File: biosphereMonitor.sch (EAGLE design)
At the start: 34 parts, among them IC1 XMEGA32A4AU, IC2 LM35, IC3 FT232RL, Q1 16Mhz, Q2 32kHz

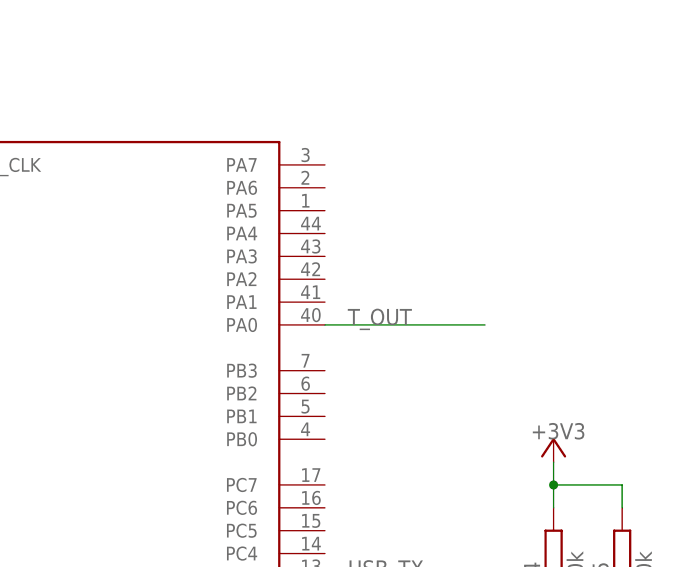
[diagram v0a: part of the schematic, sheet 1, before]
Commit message: added adc input for humidity and illuminance
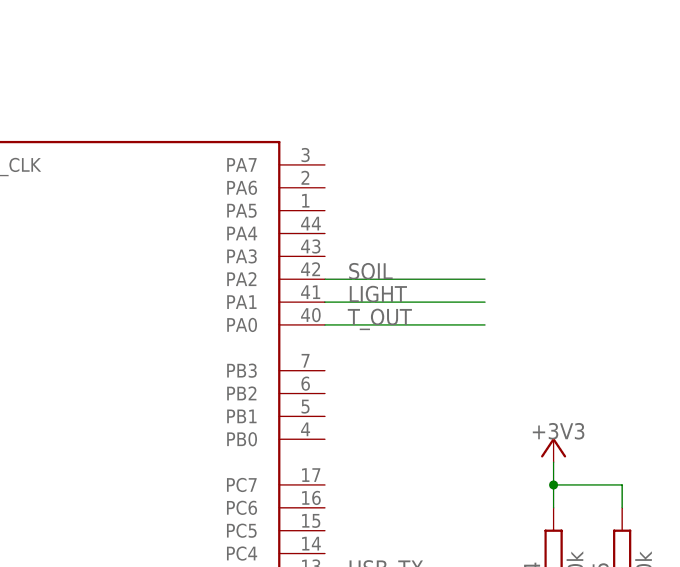
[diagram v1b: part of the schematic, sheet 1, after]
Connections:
- new net LIGHT: IC1.PA1
- new net SOIL: IC1.PA2
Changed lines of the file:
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@@
+</segment>
+</net>
+<net name="LIGHT" class="0">
+<segment>
+<pinref part="IC1" gate="G$1" pin="PA1"/>
+<wire x1="27.94" y1="22.86" x2="45.72" y2="22.86" width="0.1524" layer="91"/>
+<label x="30.48" y="22.86" size="1.778" layer="95"/>
+</segment>
+</net>
+<net name="SOIL" class="0">
+<segment>
+<pinref part="IC1" gate="G$1" pin="PA2"/>
+<wire x1="27.94" y1="25.4" x2="45.72" y2="25.4" width="0.1524" layer="91"/>
+<label x="30.48" y="25.4" size="1.778" layer="95"/>
 </segment>
 </net>

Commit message: Defined Board Shape
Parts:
- added JP4: SOIL, pinhead:PINHD-1X3
- JP2: value (none) -> PDI
- JP3: value (none) -> BME
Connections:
- net +5V: now also JP4.2
- net GND: now also JP4.3
- net SOIL: now also JP4.1
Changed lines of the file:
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@@
 <parts>
 <part name="IC1" library="atmel" library_urn="urn:adsk.eagle:library:105" deviceset="XMEGA16A4" device="A" package3d_urn="urn:adsk.eagle:package:4319/1" value="XMEGA32A4AU"/>
-<part name="JP2" library="con-harting-ml" library_urn="urn:adsk.eagle:library:149" deviceset="ML10" device="L" package3d_urn="urn:adsk.eagle:package:6964/1"/>
+<part name="JP2" library="con-harting-ml" library_urn="urn:adsk.eagle:library:149" deviceset="ML10" device="L" package3d_urn="urn:adsk.eagle:package:6964/1" value="PDI"/>
 <part name="GND1" library="supply1" library_urn="urn:adsk.eagle:library:371" deviceset="GND" device=""/>
 <part name="+3V1" library="supply1" library_urn="urn:adsk.eagle:library:371" deviceset="+3V3" device=""/>
@@
 <part name="R2" library="rcl" library_urn="urn:adsk.eagle:library:334" deviceset="R-EU_" device="R0805" package3d_urn="urn:adsk.eagle:package:23553/2" value="0"/>
 <part name="R3" library="rcl" library_urn="urn:adsk.eagle:library:334" deviceset="R-EU_" device="R0805" package3d_urn="urn:adsk.eagle:package:23553/2" value="0"/>
-<part name="JP3" library="pinhead" library_urn="urn:adsk.eagle:library:325" deviceset="PINHD-1X4" device="" package3d_urn="urn:adsk.eagle:package:22407/2"/>
+<part name="JP3" library="pinhead" library_urn="urn:adsk.eagle:library:325" deviceset="PINHD-1X4" device="" package3d_urn="urn:adsk.eagle:package:22407/2" value="BME"/>
 <part name="GND10" library="supply1" library_urn="urn:adsk.eagle:library:371" deviceset="GND" device=""/>
 <part name="+3V7" library="supply1" library_urn="urn:adsk.eagle:library:371" deviceset="+3V3" device=""/>
@@
 <part name="TP5" library="testpad" library_urn="urn:adsk.eagle:library:385" deviceset="PTR1" device="B2,54" package3d_urn="urn:adsk.eagle:package:27948/1"/>
 <part name="TP6" library="testpad" library_urn="urn:adsk.eagle:library:385" deviceset="PTR1" device="B2,54" package3d_urn="urn:adsk.eagle:package:27948/1"/>
+<part name="JP4" library="pinhead" library_urn="urn:adsk.eagle:library:325" deviceset="PINHD-1X3" device="" package3d_urn="urn:adsk.eagle:package:22458/2" value="SOIL"/>
+<part name="GND12" library="supply1" library_urn="urn:adsk.eagle:library:371" deviceset="GND" device=""/>
+<part name="P+6" library="supply1" library_urn="urn:adsk.eagle:library:371" deviceset="+5V" device=""/>
 </parts>
 <sheets>
@@
 </sheet>
 <sheet>
+<description>Inside Sensors</description>
 <plain>
 </plain>
@@
 <attribute name="VALUE" x="-25.4" y="20.32" size="1.778" layer="96"/>
 </instance>
+<instance part="JP4" gate="A" x="2.54" y="-20.32" smashed="yes">
+<attribute name="NAME" x="-3.81" y="-14.605" size="1.778" layer="95"/>
+<attribute name="VALUE" x="-3.81" y="-27.94" size="1.778" layer="96"/>
+</instance>
+<instance part="GND12" gate="1" x="-22.86" y="-27.94" smashed="yes">
+<attribute name="VALUE" x="-25.4" y="-30.48" size="1.778" layer="96"/>
+</instance>
+<instance part="P+6" gate="1" x="-22.86" y="-10.16" smashed="yes">
+<attribute name="VALUE" x="-25.4" y="-10.16" size="1.778" layer="96"/>
+</instance>
 </instances>
 <busses>
@@
 <wire x1="-22.86" y1="5.08" x2="-22.86" y2="12.7" width="0.1524" layer="91"/>
 </segment>
-</net>
+<segment>
+<pinref part="JP4" gate="A" pin="3"/>
+<pinref part="GND12" gate="1" pin="GND"/>
+<wire x1="0" y1="-22.86" x2="-22.86" y2="-22.86" width="0.1524" layer="91"/>
+<wire x1="-22.86" y1="-22.86" x2="-22.86" y2="-25.4" width="0.1524" layer="91"/>
+</segment>
+</net>
+<net name="+5V" class="0">
+<segment>
+<pinref part="JP4" gate="A" pin="2"/>
+<pinref part="P+6" gate="1" pin="+5V"/>
+<wire x1="0" y1="-20.32" x2="-22.86" y2="-20.32" width="0.1524" layer="91"/>
+<wire x1="-22.86" y1="-20.32" x2="-22.86" y2="-12.7" width="0.1524" layer="91"/>
+</segment>
+</net>
+<net name="SOIL" class="0">
+<segment>
+<pinref part="JP4" gate="A" pin="1"/>
+<wire x1="0" y1="-17.78" x2="-20.32" y2="-17.78" width="0.1524" layer="91"/>
+<label x="-20.32" y="-17.78" size="1.778" layer="95"/>
+</segment>
+</net>

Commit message: added light sensor to schematic
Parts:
- added D1: LM4050 2.5, Tjarks_Bauteile (1):LM4040
- added PH1: BPW 96C TEL, photo-elements:A1050_13
- added R6: 1k, rcl:R-EU_R0805
- added R7: 2k2, rcl:R-EU_R0805
- added R8: 3k3, rcl:R-EU_R0805
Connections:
- new net 2.5V: D1.C, R6.1, R8.2
- net +5V: now also R6.2
- net GND: now also D1.A, PH1.2, R7.1
- net LIGHT: now also PH1.1, R7.2, R8.1
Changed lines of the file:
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@@
 <part name="GND12" library="supply1" library_urn="urn:adsk.eagle:library:371" deviceset="GND" device=""/>
 <part name="P+6" library="supply1" library_urn="urn:adsk.eagle:library:371" deviceset="+5V" device=""/>
+<part name="D1" library="Tjarks_Bauteile (1)" deviceset="LM4040" device="" value="LM4050 2.5"/>
+<part name="GND13" library="supply1" library_urn="urn:adsk.eagle:library:371" deviceset="GND" device=""/>
+<part name="R6" library="rcl" library_urn="urn:adsk.eagle:library:334" deviceset="R-EU_" device="R0805" package3d_urn="urn:adsk.eagle:package:23553/2" value="1k"/>
+<part name="P+7" library="supply1" library_urn="urn:adsk.eagle:library:371" deviceset="+5V" device=""/>
+<part name="PH1" library="photo-elements" library_urn="urn:adsk.eagle:library:323" deviceset="A10" device="" package3d_urn="urn:adsk.eagle:package:22201/1" technology="50_13" value="BPW 96C TEL"/>
+<part name="R7" library="rcl" library_urn="urn:adsk.eagle:library:334" deviceset="R-EU_" device="R0805" package3d_urn="urn:adsk.eagle:package:23553/2" value="2k2"/>
+<part name="R8" library="rcl" library_urn="urn:adsk.eagle:library:334" deviceset="R-EU_" device="R0805" package3d_urn="urn:adsk.eagle:package:23553/2" value="3k3"/>
+<part name="GND14" library="supply1" library_urn="urn:adsk.eagle:library:371" deviceset="GND" device=""/>
 </parts>
 <sheets>
@@
 <attribute name="NAME" x="-34.29" y="-9.144" size="1.778" layer="95"/>
 <attribute name="TP_SIGNAL_NAME" x="-29.21" y="-2.54" size="1.778" layer="97"/>
+</instance>
+<instance part="D1" gate="G$1" x="71.12" y="-17.78" smashed="yes" rot="R90">
+<attribute name="NAME" x="68.4784" y="-20.7264" size="1.778" layer="95" rot="R90"/>
+<attribute name="VALUE" x="74.2696" y="-22.2758" size="1.778" layer="96"/>
+</instance>
+<instance part="GND13" gate="1" x="71.12" y="-27.94" smashed="yes">
+<attribute name="VALUE" x="68.58" y="-30.48" size="1.778" layer="96"/>
+</instance>
+<instance part="R6" gate="G$1" x="71.12" y="-2.54" smashed="yes" rot="R90">
+<attribute name="NAME" x="69.6214" y="-6.35" size="1.778" layer="95" rot="R90"/>
+<attribute name="VALUE" x="74.422" y="-6.35" size="1.778" layer="96" rot="R90"/>
+</instance>
+<instance part="P+7" gate="1" x="71.12" y="7.62" smashed="yes">
+<attribute name="VALUE" x="68.58" y="7.62" size="1.778" layer="96"/>
 </instance>
 </instances>
@@
 <wire x1="-45.72" y1="2.54" x2="-45.72" y2="5.08" width="0.1524" layer="91"/>
 </segment>
+<segment>
+<pinref part="GND13" gate="1" pin="GND"/>
+<pinref part="D1" gate="G$1" pin="A"/>
+<wire x1="71.12" y1="-25.4" x2="71.12" y2="-20.32" width="0.1524" layer="91"/>
+</segment>
 </net>
 <net name="+3V3" class="0">
@@
 <wire x1="-30.48" y1="2.54" x2="-30.48" y2="5.08" width="0.1524" layer="91"/>
 </segment>
+<segment>
+<pinref part="R6" gate="G$1" pin="2"/>
+<pinref part="P+7" gate="1" pin="+5V"/>
+<wire x1="71.12" y1="2.54" x2="71.12" y2="5.08" width="0.1524" layer="91"/>
+</segment>
+</net>
+<net name="2.5V" class="0">
+<segment>
+<pinref part="D1" gate="G$1" pin="C"/>
+<pinref part="R6" gate="G$1" pin="1"/>
+<wire x1="71.12" y1="-15.24" x2="71.12" y2="-10.16" width="0.1524" layer="91"/>
+<wire x1="71.12" y1="-10.16" x2="71.12" y2="-7.62" width="0.1524" layer="91"/>
+<wire x1="71.12" y1="-10.16" x2="81.28" y2="-10.16" width="0.1524" layer="91"/>
+<junction x="71.12" y="-10.16"/>
+<label x="76.2" y="-10.16" size="1.778" layer="95"/>
+</segment>
 </net>
 </nets>
@@
 <attribute name="TP_SIGNAL_NAME" x="29.21" y="30.48" size="1.778" layer="97"/>
 </instance>
+<instance part="PH1" gate="G$1" x="0" y="-17.78" smashed="yes">
+<attribute name="NAME" x="2.54" y="-17.78" size="1.778" layer="95"/>
+<attribute name="VALUE" x="2.54" y="-20.32" size="1.778" layer="96"/>
+</instance>
+<instance part="R7" gate="G$1" x="-10.16" y="-17.78" smashed="yes" rot="R90">
+<attribute name="NAME" x="-11.6586" y="-21.59" size="1.778" layer="95" rot="R90"/>
+<attribute name="VALUE" x="-6.858" y="-21.59" size="1.778" layer="96" rot="R90"/>
+</instance>
+<instance part="R8" gate="G$1" x="-10.16" y="-2.54" smashed="yes" rot="R90">
+<attribute name="NAME" x="-11.6586" y="-6.35" size="1.778" layer="95" rot="R90"/>
+<attribute name="VALUE" x="-6.858" y="-6.35" size="1.778" layer="96" rot="R90"/>
+</instance>
+<instance part="GND14" gate="1" x="-10.16" y="-30.48" smashed="yes">
+<attribute name="VALUE" x="-12.7" y="-33.02" size="1.778" layer="96"/>
+</instance>
 </instances>
 <busses>
@@
 <wire x1="-12.7" y1="25.4" x2="0" y2="25.4" width="0.1524" layer="91"/>
 </segment>
+<segment>
+<pinref part="GND14" gate="1" pin="GND"/>
+<pinref part="R7" gate="G$1" pin="1"/>
+<wire x1="-10.16" y1="-27.94" x2="-10.16" y2="-25.4" width="0.1524" layer="91"/>
+<pinref part="PH1" gate="G$1" pin="2"/>
+<wire x1="-10.16" y1="-25.4" x2="-10.16" y2="-22.86" width="0.1524" layer="91"/>
+<wire x1="0" y1="-22.86" x2="0" y2="-25.4" width="0.1524" layer="91"/>
+<wire x1="0" y1="-25.4" x2="-10.16" y2="-25.4" width="0.1524" layer="91"/>
+<junction x="-10.16" y="-25.4"/>
+</segment>
 </net>
 <net name="T_OUT" class="0">
@@
 </segment>
 </net>
+<net name="2.5V" class="0">
+<segment>
+<pinref part="R8" gate="G$1" pin="2"/>
+<wire x1="-10.16" y1="2.54" x2="-10.16" y2="5.08" width="0.1524" layer="91"/>
+<wire x1="-10.16" y1="5.08" x2="-17.78" y2="5.08" width="0.1524" layer="91"/>
+<label x="-17.78" y="5.08" size="1.778" layer="95"/>
+</segment>
+</net>
+<net name="LIGHT" class="0">
+<segment>
+<pinref part="PH1" gate="G$1" pin="1"/>
+<wire x1="0" y1="-12.7" x2="0" y2="-10.16" width="0.1524" layer="91"/>
+<wire x1="0" y1="-10.16" x2="-10.16" y2="-10.16" width="0.1524" layer="91"/>
+<pinref part="R7" gate="G$1" pin="2"/>
+<wire x1="-10.16" y1="-10.16" x2="-10.16" y2="-12.7" width="0.1524" layer="91"/>
+<pinref part="R8" gate="G$1" pin="1"/>
+<wire x1="-10.16" y1="-7.62" x2="-10.16" y2="-10.16" width="0.1524" layer="91"/>
+<junction x="-10.16" y="-10.16"/>
+<wire x1="0" y1="-10.16" x2="12.7" y2="-10.16" width="0.1524" layer="91"/>
+<junction x="0" y="-10.16"/>
+<label x="5.08" y="-10.16" size="1.778" layer="95"/>
+</segment>
+</net>

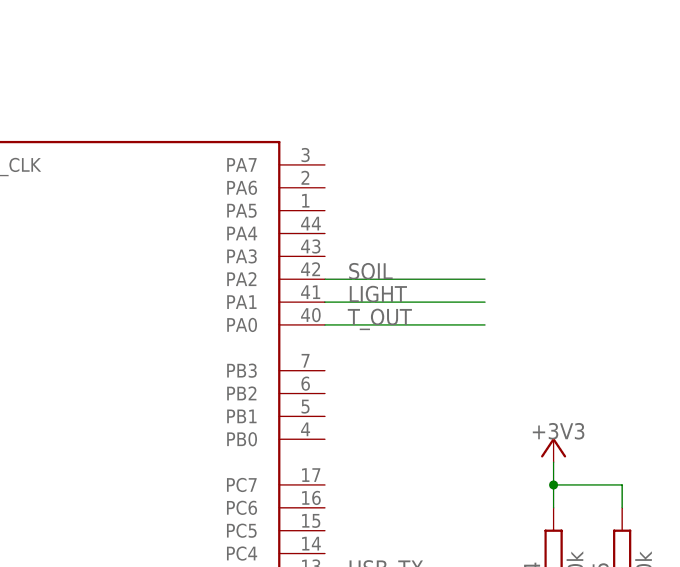
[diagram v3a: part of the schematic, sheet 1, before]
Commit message: added reference in schematic
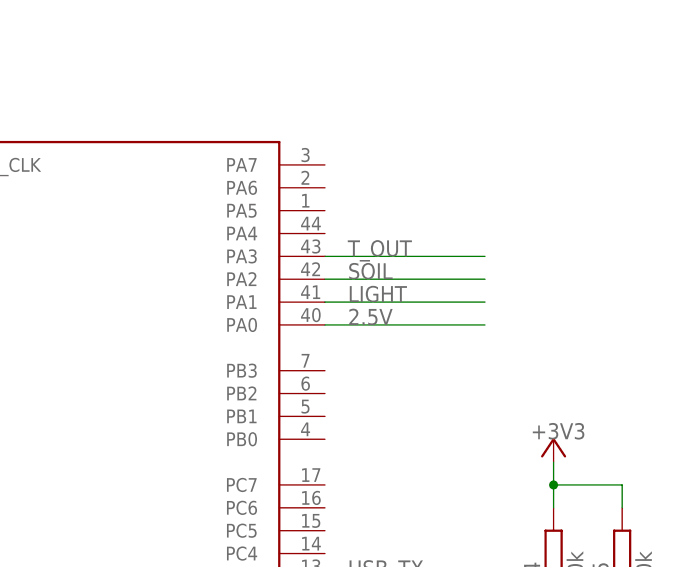
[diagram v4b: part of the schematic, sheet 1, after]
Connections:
- net 2.5V: now also IC1.PA0
- net T_OUT: now also IC1.PA3; no longer IC1.PA0
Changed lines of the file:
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@@
 <net name="T_OUT" class="0">
 <segment>
-<pinref part="IC1" gate="G$1" pin="PA0"/>
-<wire x1="45.72" y1="20.32" x2="27.94" y2="20.32" width="0.1524" layer="91"/>
-<label x="30.48" y="20.32" size="1.778" layer="95"/>
+<pinref part="IC1" gate="G$1" pin="PA3"/>
+<wire x1="27.94" y1="27.94" x2="45.72" y2="27.94" width="0.1524" layer="91"/>
+<label x="30.48" y="27.94" size="1.778" layer="95"/>
 </segment>
 </net>
@@
 </segment>
 </net>
+<net name="2.5V" class="0">
+<segment>
+<pinref part="IC1" gate="G$1" pin="PA0"/>
+<wire x1="45.72" y1="20.32" x2="27.94" y2="20.32" width="0.1524" layer="91"/>
+<label x="30.48" y="20.32" size="1.778" layer="95"/>
+</segment>
+</net>

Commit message: ups
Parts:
- added R10: 3k3, rcl:R-EU_R0805
- added R9: 2k2, rcl:R-EU_R0805
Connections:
- new net 1V: IC1.PA0, R10.1, R9.2
- net 2.5V: now also R10.2; no longer IC1.PA0
- net GND: now also R9.1
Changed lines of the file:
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@@
 <part name="R8" library="rcl" library_urn="urn:adsk.eagle:library:334" deviceset="R-EU_" device="R0805" package3d_urn="urn:adsk.eagle:package:23553/2" value="3k3"/>
 <part name="GND14" library="supply1" library_urn="urn:adsk.eagle:library:371" deviceset="GND" device=""/>
+<part name="R9" library="rcl" library_urn="urn:adsk.eagle:library:334" deviceset="R-EU_" device="R0805" package3d_urn="urn:adsk.eagle:package:23553/2" value="2k2"/>
+<part name="R10" library="rcl" library_urn="urn:adsk.eagle:library:334" deviceset="R-EU_" device="R0805" package3d_urn="urn:adsk.eagle:package:23553/2" value="3k3"/>
+<part name="GND15" library="supply1" library_urn="urn:adsk.eagle:library:371" deviceset="GND" device=""/>
 </parts>
 <sheets>
@@
 <instance part="+3V8" gate="G$1" x="53.34" y="7.62" smashed="yes">
 <attribute name="VALUE" x="50.8" y="7.62" size="1.778" layer="96"/>
+</instance>
+<instance part="R9" gate="G$1" x="71.12" y="12.7" smashed="yes" rot="R90">
+<attribute name="NAME" x="69.6214" y="8.89" size="1.778" layer="95" rot="R90"/>
+<attribute name="VALUE" x="74.422" y="8.89" size="1.778" layer="96" rot="R90"/>
+</instance>
+<instance part="R10" gate="G$1" x="71.12" y="27.94" smashed="yes" rot="R90">
+<attribute name="NAME" x="69.6214" y="24.13" size="1.778" layer="95" rot="R90"/>
+<attribute name="VALUE" x="74.422" y="24.13" size="1.778" layer="96" rot="R90"/>
+</instance>
+<instance part="GND15" gate="1" x="71.12" y="2.54" smashed="yes">
+<attribute name="VALUE" x="68.58" y="0" size="1.778" layer="96"/>
 </instance>
 </instances>
@@
 <junction x="-53.34" y="-35.56"/>
 </segment>
+<segment>
+<pinref part="GND15" gate="1" pin="GND"/>
+<pinref part="R9" gate="G$1" pin="1"/>
+<wire x1="71.12" y1="5.08" x2="71.12" y2="7.62" width="0.1524" layer="91"/>
+</segment>
 </net>
 <net name="N$1" class="0">
@@
 <net name="2.5V" class="0">
 <segment>
+<pinref part="R10" gate="G$1" pin="2"/>
+<wire x1="71.12" y1="33.02" x2="71.12" y2="35.56" width="0.1524" layer="91"/>
+<wire x1="71.12" y1="35.56" x2="63.5" y2="35.56" width="0.1524" layer="91"/>
+<label x="63.5" y="35.56" size="1.778" layer="95"/>
+</segment>
+</net>
+<net name="1V" class="0">
+<segment>
+<pinref part="R9" gate="G$1" pin="2"/>
+<pinref part="R10" gate="G$1" pin="1"/>
+<wire x1="71.12" y1="22.86" x2="71.12" y2="20.32" width="0.1524" layer="91"/>
+<junction x="71.12" y="20.32"/>
 <pinref part="IC1" gate="G$1" pin="PA0"/>
-<wire x1="45.72" y1="20.32" x2="27.94" y2="20.32" width="0.1524" layer="91"/>
+<wire x1="27.94" y1="20.32" x2="71.12" y2="20.32" width="0.1524" layer="91"/>
+<wire x1="71.12" y1="20.32" x2="71.12" y2="17.78" width="0.1524" layer="91"/>
 <label x="30.48" y="20.32" size="1.778" layer="95"/>
 </segment>
